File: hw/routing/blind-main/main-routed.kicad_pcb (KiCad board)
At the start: 4 copper layers, 54 x 71 mm, 196 parts

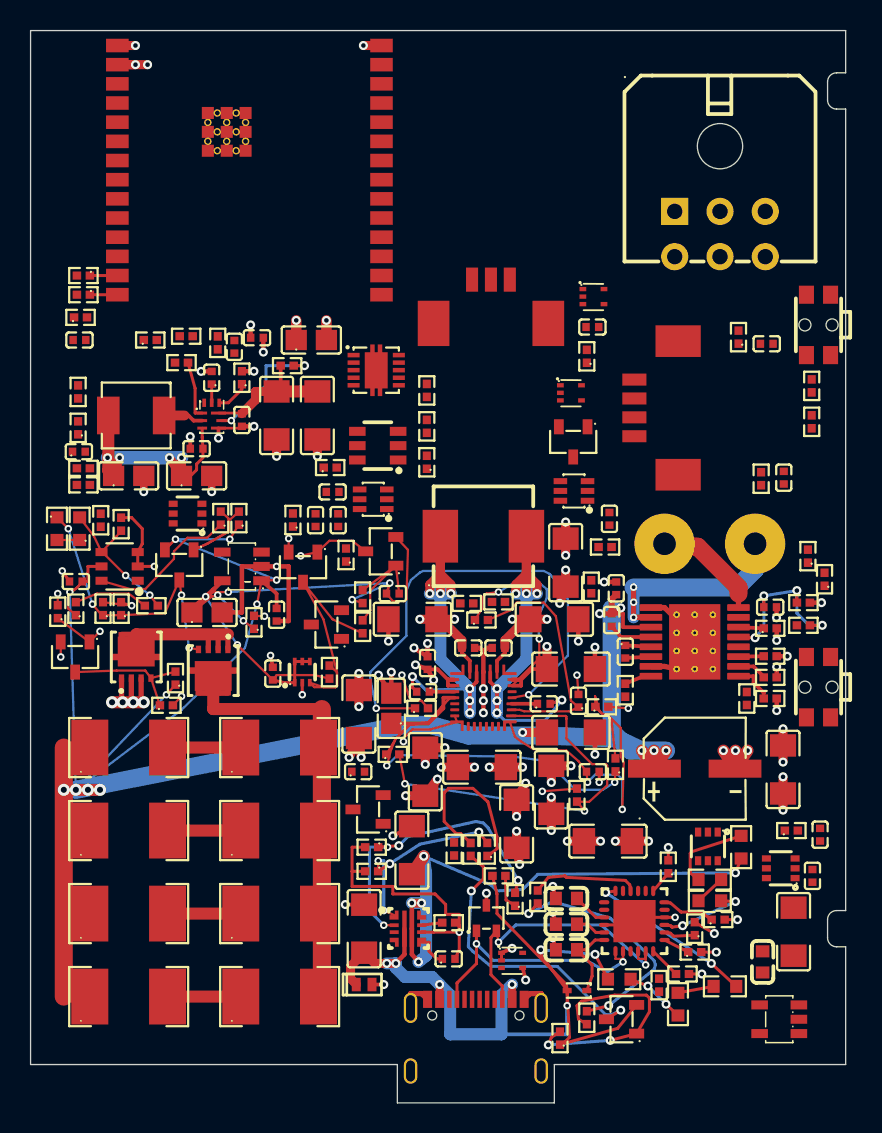
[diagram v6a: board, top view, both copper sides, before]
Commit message: Route protected USB data and render the specified black board finish
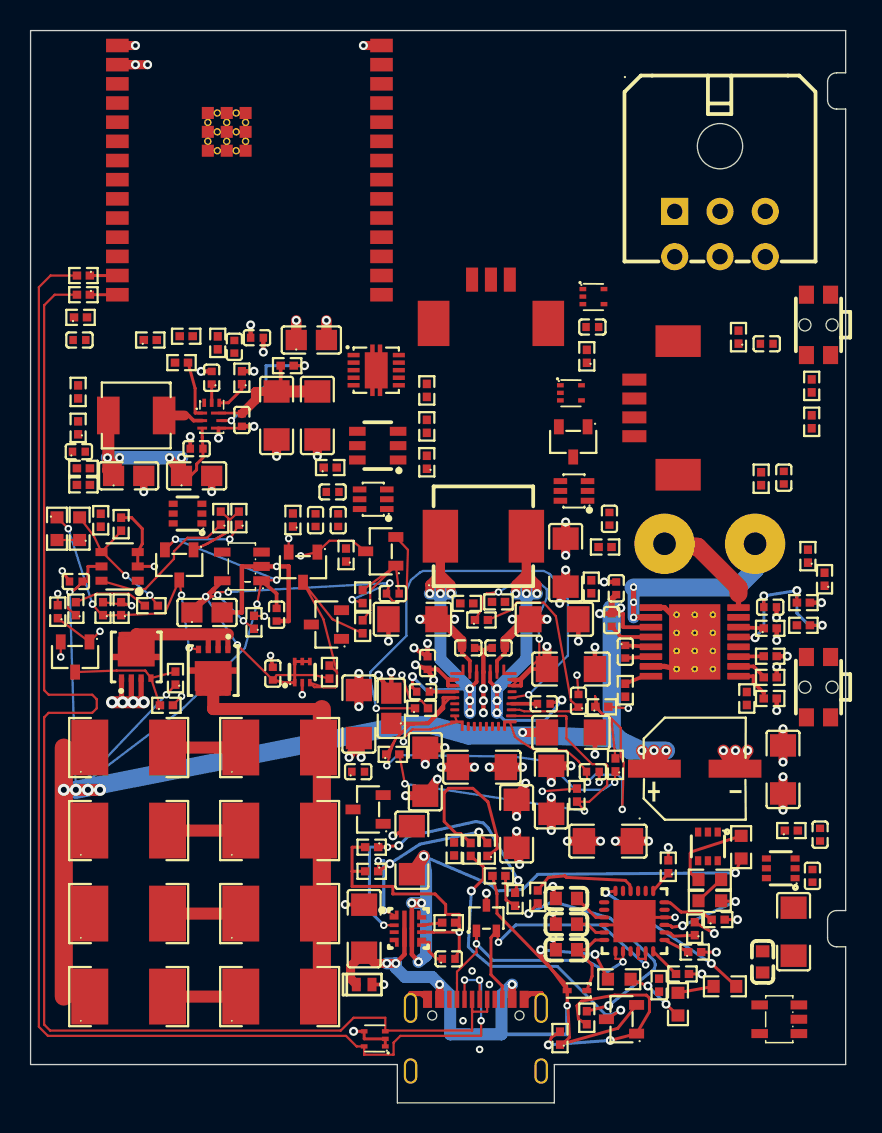
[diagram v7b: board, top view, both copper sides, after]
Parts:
- moved D2 10.5 mm to (122.8, 173.3), turned to 180 degrees
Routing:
- net usb_dp: track 0.00 -> 90.9 mm
- net usb_dm: track 0.00 -> 90.5 mm, vias 0 -> 3
- net lv: track 150.4 -> 151.4 mm, vias 86 -> 89
- added copper zone on In2.Cu, net lv

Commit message: Route local supervision and encoder returns on the protected USB board
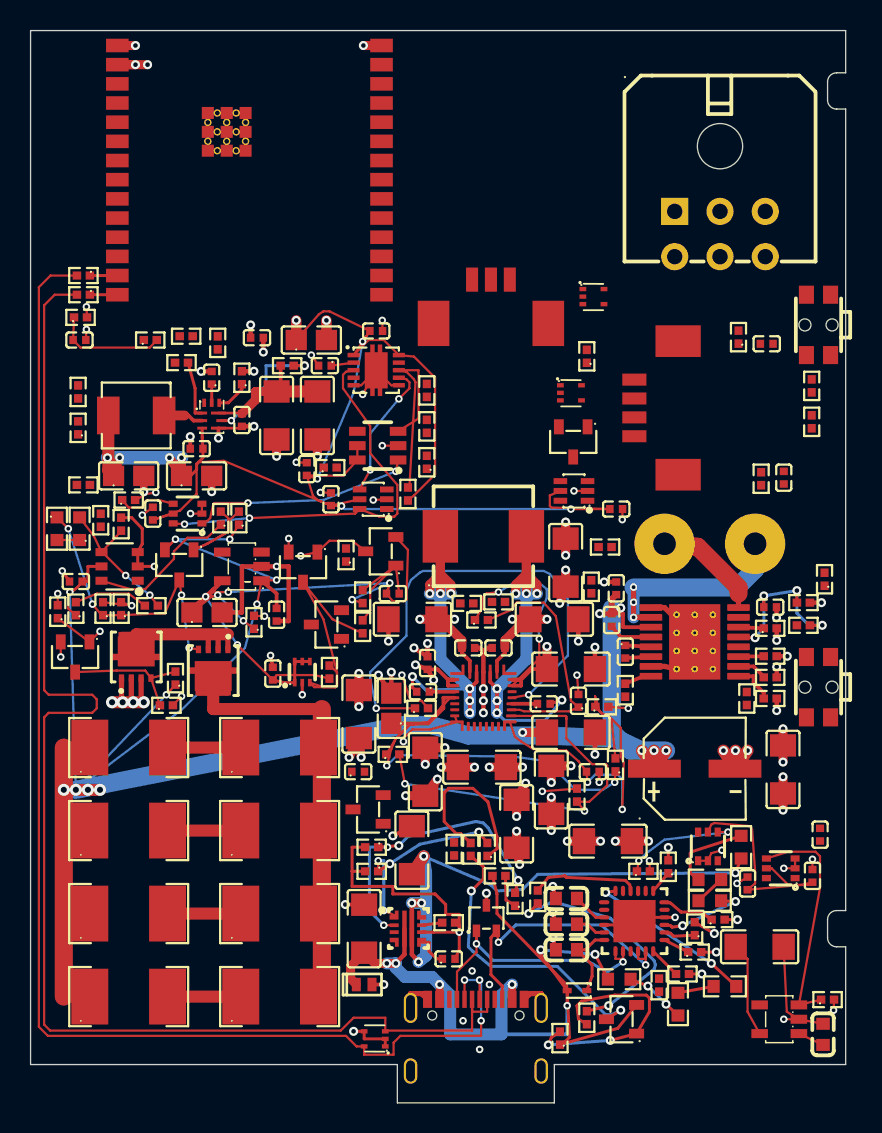
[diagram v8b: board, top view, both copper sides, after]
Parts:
- moved C23 25.8 mm to (147.5, 163.0)
- moved R39 23.6 mm to (140.6, 162.2), turned to 0 degrees
- moved R93 21.6 mm to (125.0, 137.2), turned to 90 degrees
- moved C59 17.3 mm to (119.5, 128.7), turned to 180 degrees
- moved C28 12.2 mm to (138.8, 138.2)
- moved C56 12.0 mm to (108.1, 138.5), turned to 90 degrees
- moved R68 11.5 mm to (152.8, 170.7)
- moved R91 11.0 mm to (106.5, 137.6), turned to 0 degrees
- moved C60 9.46 mm to (122.9, 126.4), turned to 0 degrees
- moved C53 6.25 mm to (152.5, 173.0)
- moved C58 3.97 mm to (118.3, 135.6)
- moved C54 2.46 mm to (148.3, 167.2), turned to 0 degrees
- moved C57 1.72 mm to (119.9, 137.6)
- turned U17 to -90 degrees
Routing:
- net rail-hv: track 60.5 -> 160.8 mm, vias 8 -> 12
- net lv: track 151.4 -> 182.8 mm, vias 89 -> 110
- net supervision-6: track 0.00 -> 26.4 mm, vias 0 -> 2
- net EN: track 0.00 -> 15.2 mm
- net reset_n: track 0.00 -> 14.9 mm, vias 0 -> 2
- net MR: track 0.00 -> 14.6 mm
- net WDI: track 0.00 -> 9.04 mm, vias 0 -> 2
- net Y: track 1.67 -> 9.49 mm, vias 0 -> 2
- net c_adc-1: track 0.00 -> 7.47 mm
- net encoder-output-hv: track 0.00 -> 6.28 mm
- net motor_sleep_n-Y: track 0.00 -> 3.94 mm
- net source-hv: track 68.4 -> 70.1 mm
- net CWD: track 0.00 -> 1.49 mm
